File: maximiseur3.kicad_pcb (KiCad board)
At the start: 2 copper layers, 70.4 x 50 mm, 31 parts, among them P1 M- PV- M+ PV+, P2 SW SW, Q1 IRLB3036G, Q2 IRLB3036G, Q3 IRLB3036G, Q4 IRLB3036G, T1 BD139, U1 LM358

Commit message: work in progress
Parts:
- removed the D1 at (101.3, 51.0)
- removed P2: SW SW, maximiseur:bornier2
- added C10: 1000µF, maximiseur:CP_Radial_D16.0mm_P7.50mm, F.Cu at (51.8, 20.5)
- added C7: 1000µF, maximiseur:CP_Radial_D16.0mm_P7.50mm, F.Cu at (105.6, 20.5)
- added C8: 1000µF, maximiseur:CP_Radial_D16.0mm_P7.50mm, F.Cu at (87.6, 20.5)
- added C9: 1000µF, maximiseur:CP_Radial_D16.0mm_P7.50mm, F.Cu at (69.6, 20.5)
- added D4: MUR420RL, maximiseur:D_DO-201AE_P15.24mm_Horizontal, F.Cu at (114.6, 51.5)
- added J1: PV+/M+, maximiseur:7808, F.Cu at (33.6, 25.3)
- added J2: M-, maximiseur:7808, F.Cu at (33.6, 66.3)
- added J3: PV-, maximiseur:7808, F.Cu at (33.6, 2.29)
- C1: footprint maximiseur:C_Radial_D5_L6_P2.5 -> Capacitor_THT:C_Disc_D10.0mm_W2.5mm_P5.00mm
- C3, C4, C5, C6: value 470µF -> 1000µF; footprint maximiseur:C_Radial_D22_L41_P10 -> maximiseur:CP_Radial_D16.0mm_P7.50mm
- D1, D2, D3: value SF52 -> MUR420RL; footprint maximiseur:D6.5 -> maximiseur:D_DO-201AE_P15.24mm_Horizontal
- P1: value M- PV- M+ PV+ -> SW SW; footprint maximiseur:bornier4 -> maximiseur:bornier2
- U1: value LM358 -> LM311
- moved P1 47.4 mm to (23.5, 90.2)
- moved C1 24.4 mm to (98.1, 74.3)
- moved D2 15.0 mm to (28.3, 38.0), turned to 270 degrees
- moved C4 15.0 mm to (105.6, 30.5)
- moved R2 14.7 mm to (105.9, 69.4)
- moved C2 14.7 mm to (78.5, 77.0)
- moved DZ2 14.7 mm to (92.0, 59.2)
- moved R3 14.7 mm to (94.5, 59.2)
- moved R4 14.7 mm to (105.9, 73.2)
- moved R5 14.7 mm to (82.0, 74.5)
- moved R6 14.7 mm to (105.9, 77.0)
- moved U1 14.7 mm to (90.7, 71.9)
- moved RV1 14.7 mm to (108.5, 65.8)
- moved C3 10.0 mm to (87.6, 30.5)
- moved Q4 7.16 mm to (74.1, 54.5)
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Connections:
- P1 pad 1: /M- -> /PV-
- P1 pad 2: /PV- -> /RC
- U1 pad 1: Net-(C2-Pad1) -> /PV-
- U1 pad 2: Net-(DZ2-Pad1) -> /RC
- U1 pad 3: /RC -> Net-(DZ2-Pad1)
- U1 pad 5: (no net) -> Net-(U1-Pad5)
- U1 pad 6: (no net) -> Net-(U1-Pad5)
- U1 pad 7: (no net) -> Net-(C2-Pad1)
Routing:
- net /RC: track 62.3 -> 35.9 mm, vias 2 -> 0
- net /PV-: track 27.9 -> 13.2 mm
- net Net-(DZ2-Pad1): track 20.9 -> 6.35 mm
- net Net-(C2-Pad1): track 58.9 -> 55.6 mm
- net /+V: track 47.8 -> 50.8 mm
- net Net-(U1-Pad5): track 0.00 -> 2.54 mm
- removed copper zone on B.Cu, net /M+
- removed copper zone on B.Cu, net /PV-
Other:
- board outline removed
- board text removed: "M-|PV-|PV+ M+"

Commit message: work in progress
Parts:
- moved DZ1 86.3 mm to (143.9, 76.7), turned to 270 degrees
- moved R1 78.6 mm to (135.6, 80.4), turned to 0 degrees
- moved R10 69.8 mm to (113.4, 92.1), turned to 90 degrees
- moved Q3 56.9 mm to (106.0, 83.1)
- moved Q2 56.0 mm to (96.2, 83.1)
- moved R8 55.1 mm to (98.6, 92.1), turned to 90 degrees
- moved R9 55.0 mm to (108.7, 92.1), turned to 90 degrees
- moved D2 51.7 mm to (63.6, 75.8)
- moved Q4 50.5 mm to (115.7, 83.1)
- moved R2 49.8 mm to (135.6, 109.3), turned to 90 degrees
- moved J3 48.7 mm to (63.2, 41.0)
- moved C1 48.7 mm to (127.7, 113.0)
- moved R3 48.7 mm to (124.1, 98.0)
- moved DZ2 48.7 mm to (121.5, 98.0)
- moved U1 48.7 mm to (120.3, 110.7)
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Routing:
- net /+V: track 50.8 -> 16.5 mm
- net /PV-: track 13.2 -> 35.6 mm
- net /RC: track 35.9 -> 22.8 mm
- net Net-(R3-Pad1): track 17.5 -> 6.28 mm
- net Net-(DZ2-Pad1): track 6.35 -> 17.4 mm
- net Net-(DZ1-Pad1): track 0.00 -> 10.5 mm
- net /M+: track 0.00 -> 7.32 mm
- net Net-(Q3-PadG): track 0.00 -> 3.83 mm
- net Net-(Q1-PadG): track 0.00 -> 3.61 mm
- net Net-(Q2-PadG): track 0.00 -> 3.57 mm
- net Net-(Q4-PadG): track 0.00 -> 3.55 mm
- net Net-(R2-Pad2): track 7.82 -> 4.32 mm
- added copper zone on B.Cu, net /M+
- added copper zone on B.Cu, net /PV-

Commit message: work in progress
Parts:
- added C11: 1000µF, maximiseur:CP_Radial_D16.0mm_P7.50mm, F.Cu at (118.6, 58.0)
- C1: value 0,1µF -> 10µF; footprint Capacitor_THT:C_Disc_D10.0mm_W2.5mm_P5.00mm -> Capacitor_THT:CP_Radial_D5.0mm_P2.50mm
- C2: value 100pF -> 100nF; footprint maximiseur:C_Rect_L7_W2.5_P5 -> Capacitor_THT:C_Rect_L7.0mm_W2.0mm_P5.00mm
- C3: value 1000µF -> 100pF; footprint maximiseur:CP_Radial_D16.0mm_P7.50mm -> Capacitor_THT:C_Disc_D5.0mm_W2.5mm_P2.50mm
- DZ1, DZ2: footprint maximiseur:D3 -> Diode_THT:D_DO-34_SOD68_P7.62mm_Horizontal
- R1, R10, R2, R4, R5, R6, R7, R8, R9: footprint maximiseur:R3-LARGE_PADS -> Resistor_THT:R_Axial_DIN0207_L6.3mm_D2.5mm_P7.62mm_Horizontal
- R3: value 3k3 -> 2k2; footprint maximiseur:R3-LARGE_PADS -> Resistor_THT:R_Axial_DIN0207_L6.3mm_D2.5mm_P7.62mm_Horizontal
- U1: footprint maximiseur:DIP-8__300_ELL -> Package_DIP:DIP-8_W7.62mm_LongPads
- moved P1 91.5 mm to (142.9, 111.4)
- moved C3 52.2 mm to (101.0, 107.1), turned to 90 degrees
- moved C1 25.1 mm to (143.1, 93.2)
- moved DZ2 7.86 mm to (128.4, 94.1), turned to 90 degrees
- moved R4 6.35 mm to (132.2, 115.7)
- moved R10 6.35 mm to (113.5, 98.4)
- moved R2 6.35 mm to (135.6, 115.7)
- moved R7 6.35 mm to (88.9, 98.4)
- moved R8 6.35 mm to (98.6, 98.4)
- moved R9 6.35 mm to (108.7, 98.4)
- moved U1 5.23 mm to (124.0, 106.9), turned to 270 degrees
- moved R1 3.81 mm to (131.8, 80.4)
- moved DZ1 3.74 mm to (144.5, 80.4), turned to 90 degrees
- moved R6 1.17 mm to (126.2, 117.7)
- moved C6 0.18 mm to (83.8, 57.9)
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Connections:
- C1 pad 1: /+V -> /+15V
- C2 pad 1: Net-(C2-Pad1) -> /+15V
- C2 pad 2: /RC -> /PV-
- C3 pad 1: /M+ -> Net-(C3-Pad1)
- C3 pad 2: /PV- -> /RC
- R10 pad 1: Net-(C2-Pad1) -> Net-(C3-Pad1)
- R4 pad 1: /+V -> /+15V
- R5 pad 1: Net-(C2-Pad1) -> Net-(C3-Pad1)
- R6 pad 1: /+V -> /+15V
- R6 pad 2: Net-(C2-Pad1) -> Net-(C3-Pad1)
- R7 pad 1: Net-(C2-Pad1) -> Net-(C3-Pad1)
- R8 pad 1: Net-(C2-Pad1) -> Net-(C3-Pad1)
- R9 pad 1: Net-(C2-Pad1) -> Net-(C3-Pad1)
- T1 pad 1: /+V -> /+15V
- U1 pad 7: Net-(C2-Pad1) -> Net-(C3-Pad1)
- U1 pad 8: /+V -> /+15V
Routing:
- net Net-(C2-Pad1): track 55.9 -> 21.3 mm
- net /M+: track 7.32 -> 28.0 mm, vias 0 -> 2
- net /+V: track 16.5 -> 0.00 mm
- net /RC: track 22.8 -> 15.8 mm
- net /PV-: track 35.6 -> 41.4 mm
- net Net-(DZ2-Pad1): track 17.4 -> 14.2 mm
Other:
- board text added: "+"
- board text added: "M-"
- board text added: "PV-"

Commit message: premiere version correcte du PCB
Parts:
- C3: footprint Capacitor_THT:C_Disc_D5.0mm_W2.5mm_P2.50mm -> Capacitor_THT:C_Rect_L7.0mm_W2.0mm_P5.00mm
- R1, R10, R2, R3, R4, R5, R6, R7, R8, R9: footprint Resistor_THT:R_Axial_DIN0207_L6.3mm_D2.5mm_P7.62mm_Horizontal -> Resistor_THT:R_Axial_DIN0207_L6.3mm_D2.5mm_P10.16mm_Horizontal
- moved C3 30.5 mm to (127.4, 91.9), turned to 0 degrees
- moved DZ2 25.4 mm to (114.2, 115.1), turned to 180 degrees
- moved R2 24.8 mm to (136.6, 90.9), turned to 0 degrees
- moved R3 23.9 mm to (146.8, 105.5), turned to 180 degrees
- moved R6 19.7 mm to (129.8, 98.3)
- moved C1 15.1 mm to (129.8, 86.1), turned to 180 degrees
- moved C2 14.5 mm to (127.8, 107.3), turned to 180 degrees
- moved RV1 14.2 mm to (144.4, 100.9), turned to 90 degrees
- moved R4 12.9 mm to (127.8, 103.5), turned to 180 degrees
- moved R5 12.1 mm to (125.6, 95.1)
- moved U1 5.96 mm to (120.2, 111.5), turned to 0 degrees
- moved P1 3.83 mm to (143.6, 115.1)
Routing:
- net Net-(C3-Pad1): track 0.00 -> 61.6 mm
- net /RC: track 15.8 -> 60.7 mm
- net /PV-: track 41.4 -> 0.00 mm
- net /+15V: track 0.00 -> 30.0 mm
- net Net-(C2-Pad1): track 21.3 -> 0.00 mm
- net Net-(DZ2-Pad1): track 14.2 -> 20.7 mm
- net /M+: track 28.0 -> 33.2 mm
- net Net-(R2-Pad2): track 4.32 -> 5.98 mm
- net Net-(R3-Pad1): track 6.28 -> 5.60 mm

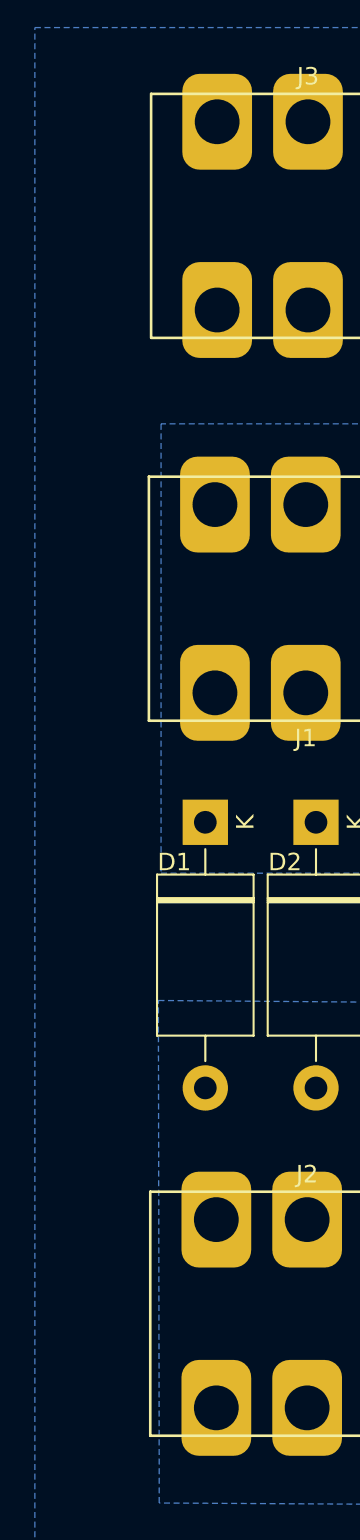
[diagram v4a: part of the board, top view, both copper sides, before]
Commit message: ajout vue 3D
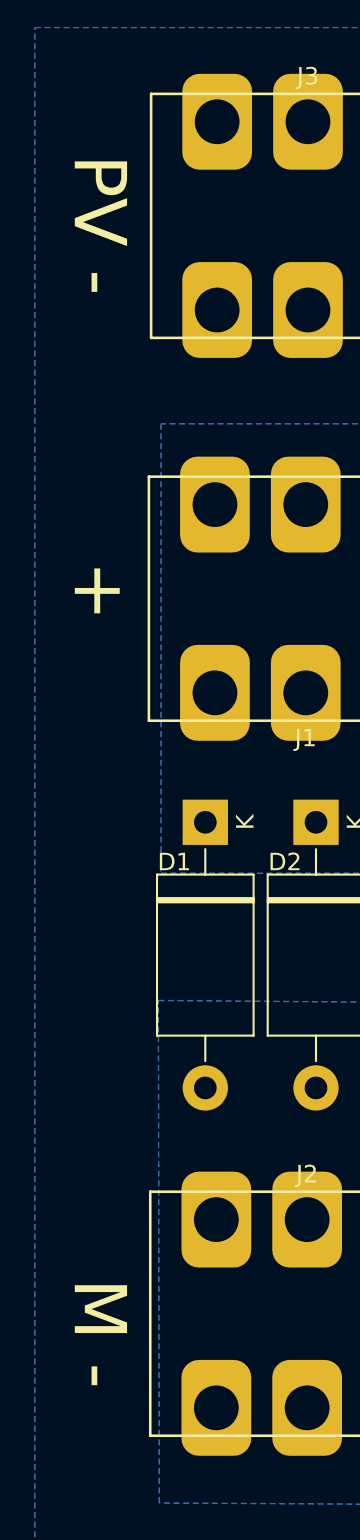
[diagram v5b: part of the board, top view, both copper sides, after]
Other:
- board text added: "M -"
- board text added: "PV -"
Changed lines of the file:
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@@
   (general
     (thickness 1.6)
-    (drawings 12)
+    (drawings 15)
     (tracks 74)
     (zones 0)
@@
     )
   )
+  (gr_text + (at 51.176 62.544 270) (layer F.SilkS)
+    (effects (font (size 3 3) (thickness 0.3)))
+  )
+  (gr_text "M -" (at 51.176 105.144 270) (layer F.SilkS)
+    (effects (font (size 3 3) (thickness 0.3)))
+  )
+  (gr_text "PV -" (at 51.176 41.544 270) (layer F.SilkS)
+    (effects (font (size 3 3) (thickness 0.3)))
+  )
   (gr_line (start 127.254 68.199) (end 127.254 74.90319) (layer F.SilkS) (width 0.15))

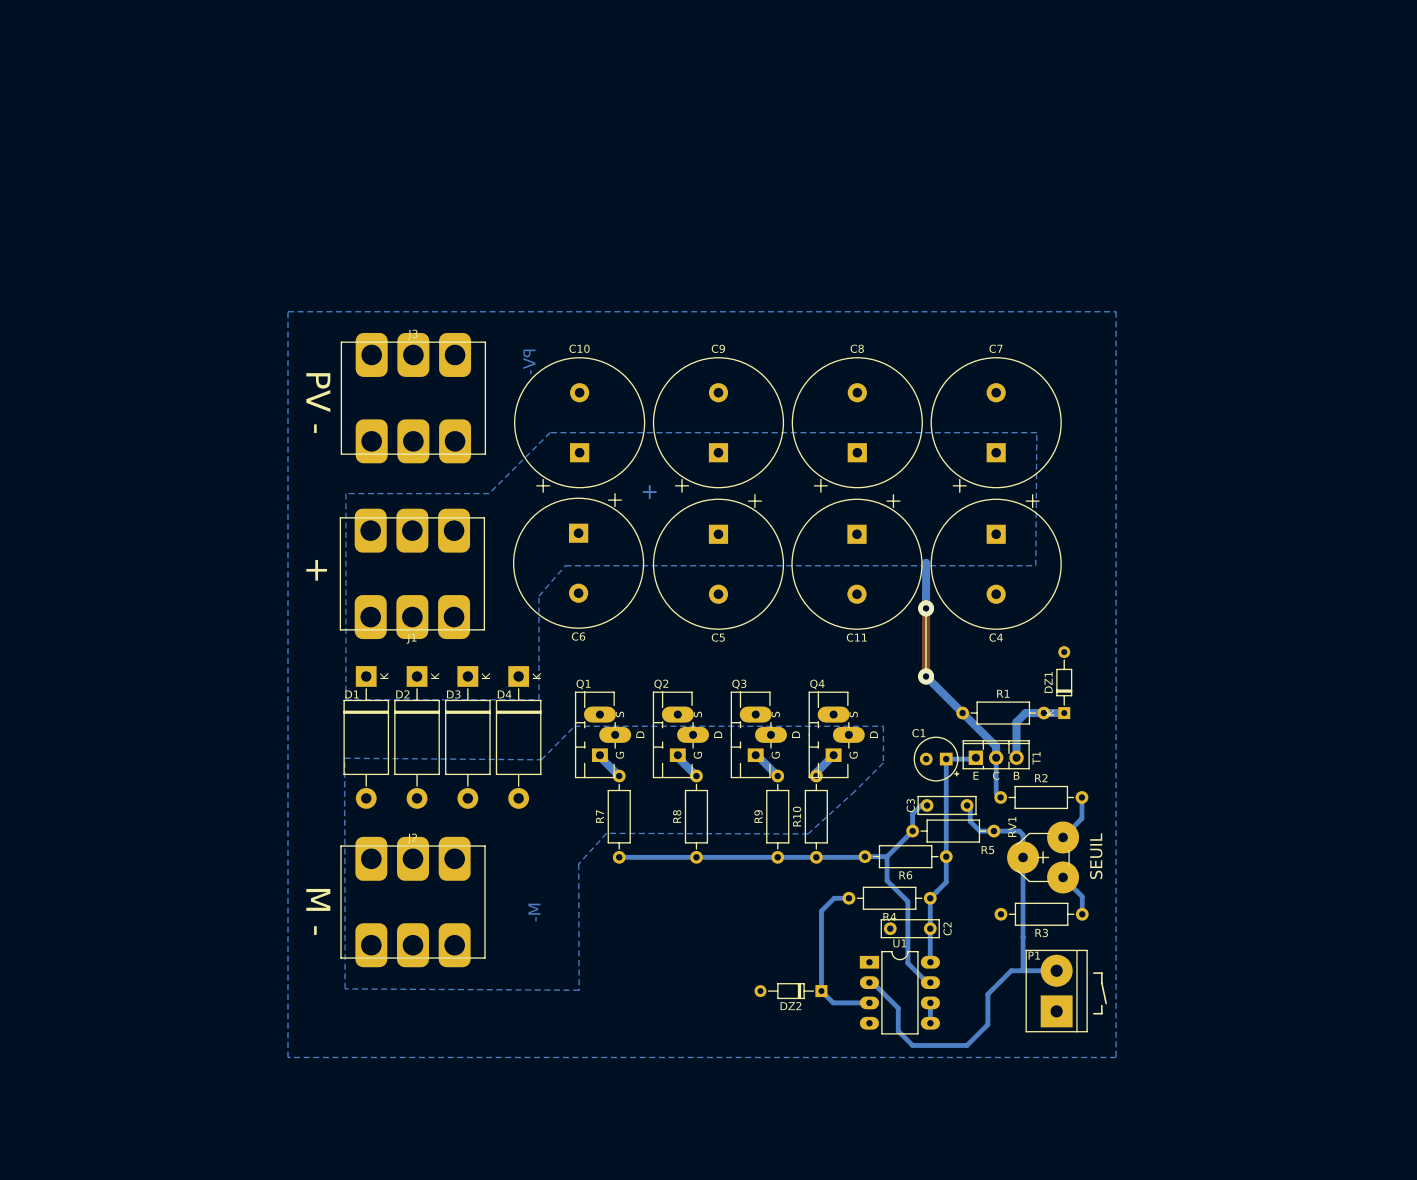
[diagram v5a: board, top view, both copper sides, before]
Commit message: ajout de varistances de protection, taille définitive du PCB
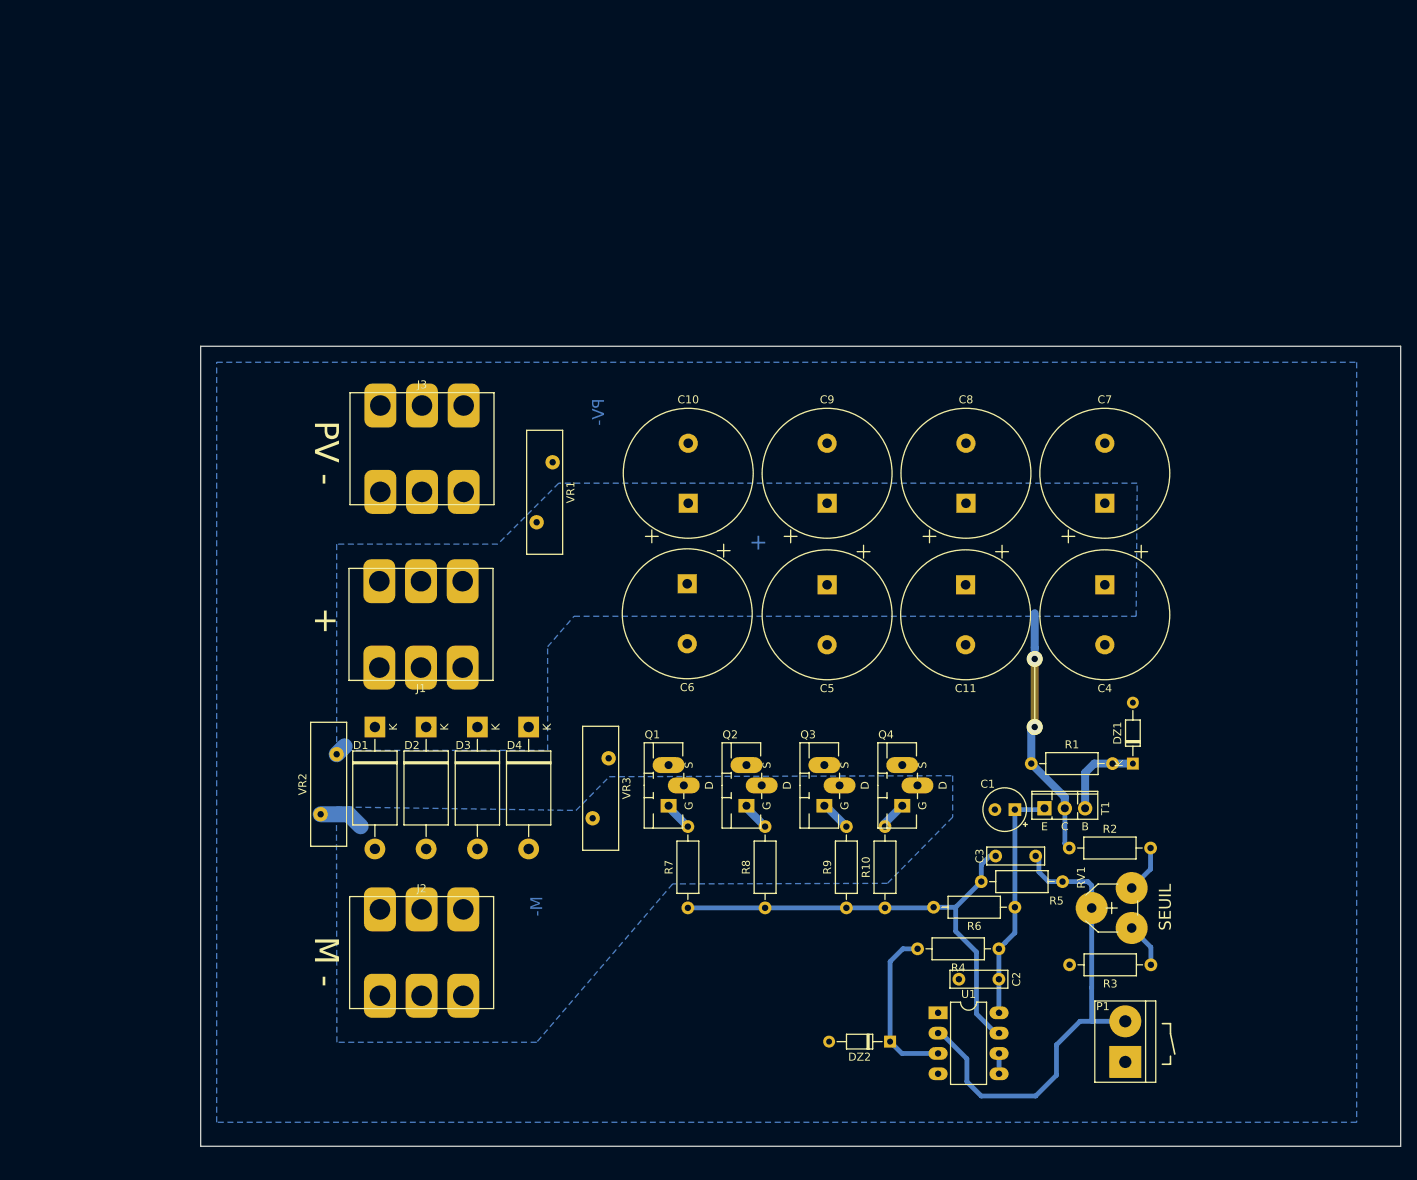
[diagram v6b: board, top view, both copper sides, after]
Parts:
- added VR1: V56ZA8, Varistor:RV_Disc_D15.5mm_W4.5mm_P7.5mm, F.Cu at (78.6, 56.5)
- added VR2: V56ZA8, Varistor:RV_Disc_D15.5mm_W4.5mm_P7.5mm, F.Cu at (53.6, 85.5)
- added VR3: V56ZA8, Varistor:RV_Disc_D15.5mm_W4.5mm_P7.5mm, F.Cu at (85.6, 93.5)
- moved C8 15.0 mm to (132.2, 54.2)
- moved C10 15.0 mm to (97.5, 54.2)
- moved C11 15.0 mm to (132.2, 64.4)
- moved C4 15.0 mm to (149.6, 64.4)
- moved C6 15.0 mm to (97.4, 64.2)
- moved C7 15.0 mm to (149.6, 54.2)
- moved C9 15.0 mm to (114.9, 54.2)
- moved C5 15.0 mm to (114.9, 64.4)
- moved C2 10.7 mm to (136.4, 113.7)
- moved R4 10.7 mm to (136.4, 109.9)
- moved R6 10.7 mm to (138.4, 104.7)
- moved RV1 10.7 mm to (153.0, 107.3)
- moved C1 10.7 mm to (138.4, 92.5)
- moved C3 10.7 mm to (136.0, 98.3)
- moved DZ1 10.7 mm to (153.1, 86.7)
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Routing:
- net /M-: track 0.00 -> 5.62 mm
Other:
- board outline added: 150 x 100 mm
